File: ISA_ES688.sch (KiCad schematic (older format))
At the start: 90 parts, among them J1 LINE IN, J11 ISA BUS, J2 LINE OUT, J3 Joystick/MIDI, J7 SPKR OUT, J8 MIC, U1 L78L05, U2 74LS14, U7 LM1877, Y1 14.318Mhz

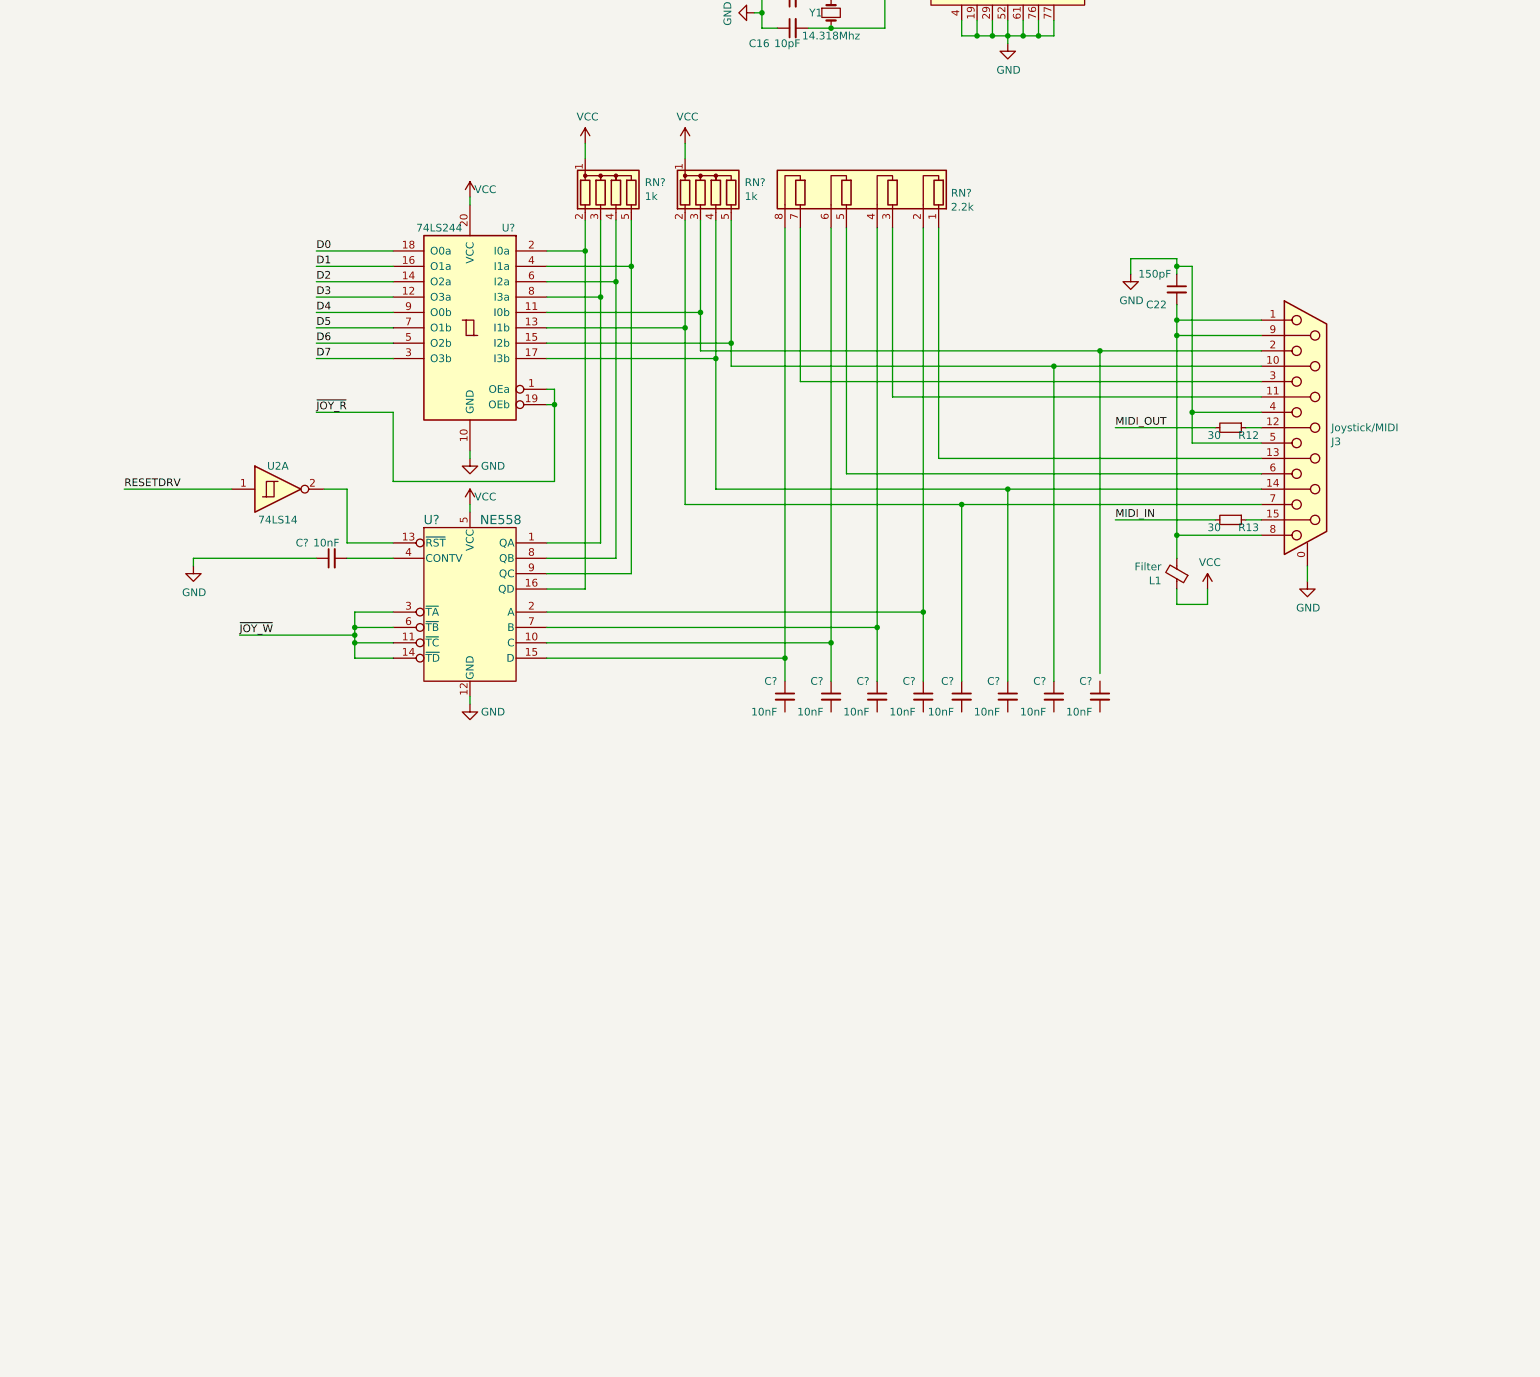
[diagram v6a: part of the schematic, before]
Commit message: Add gnd connection to caps for joystick
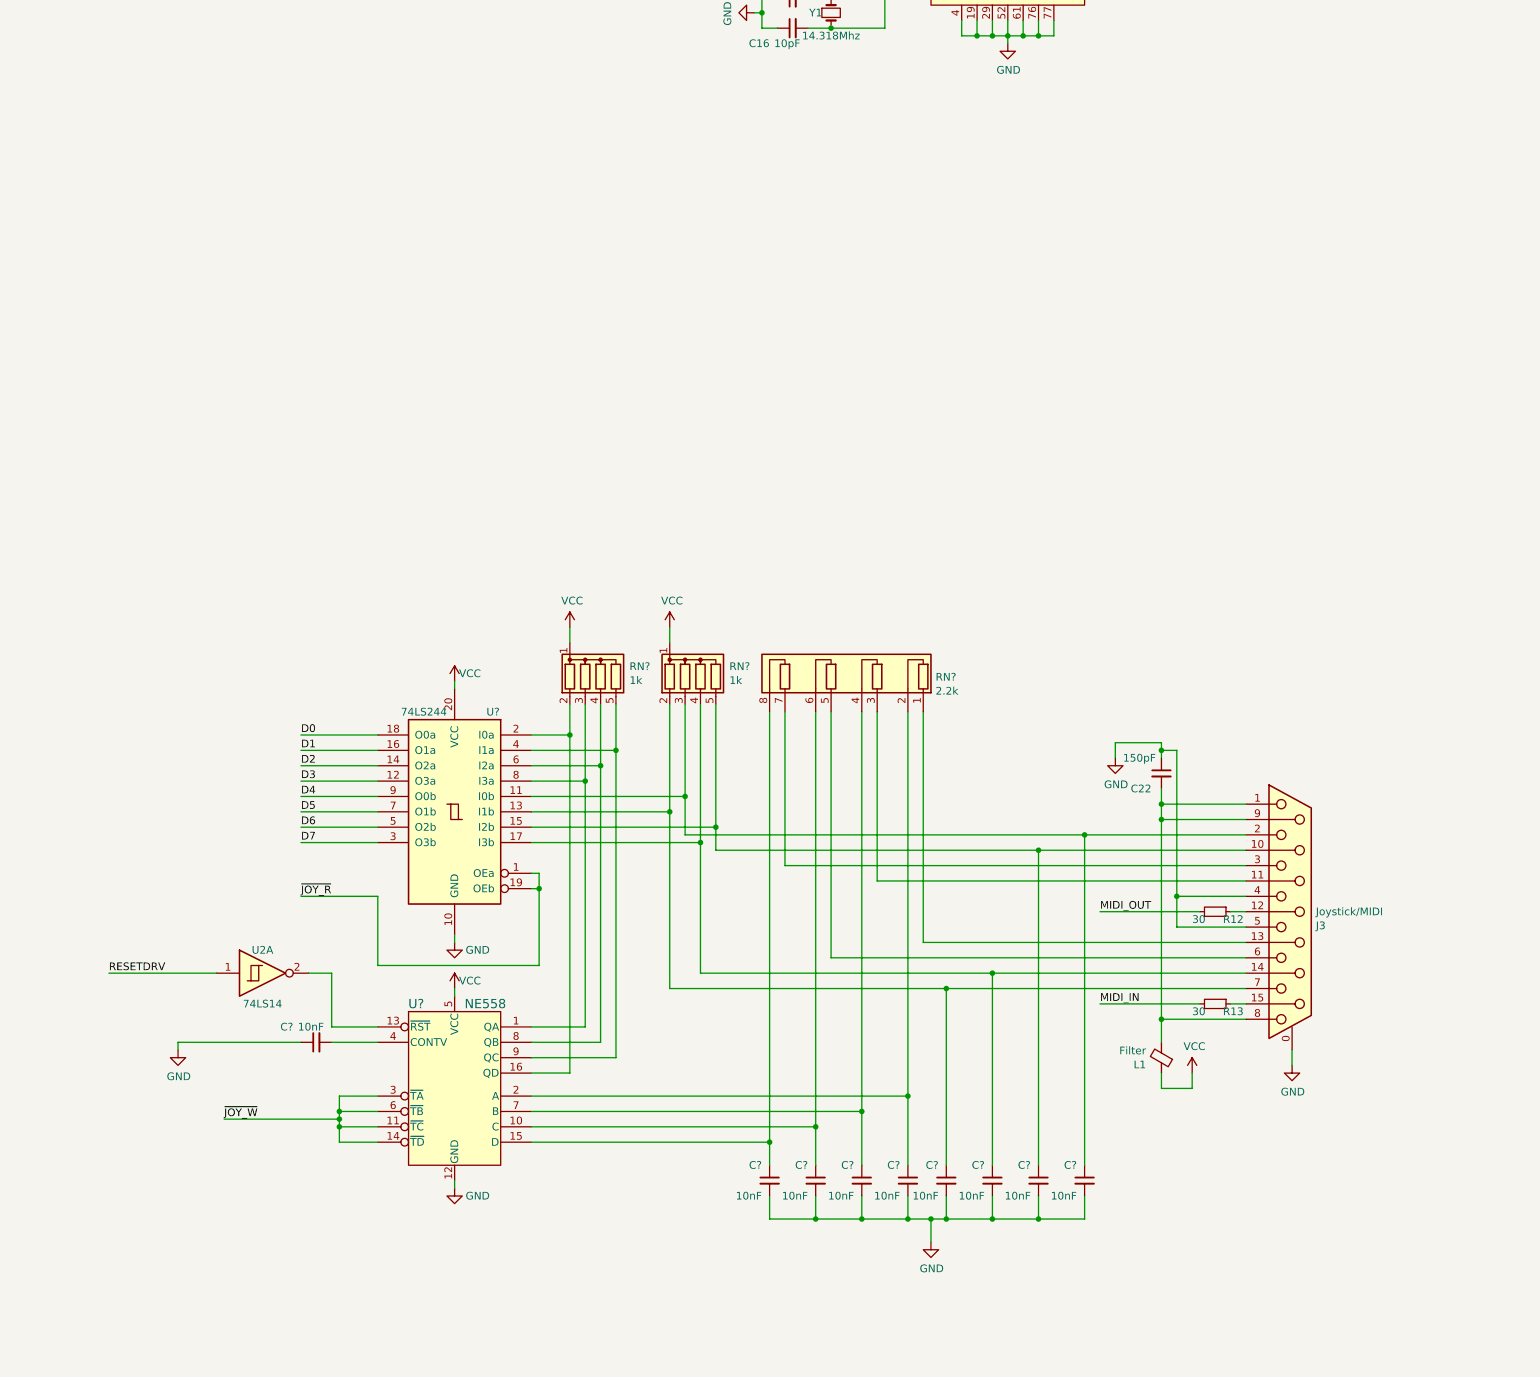
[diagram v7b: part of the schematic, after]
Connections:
- net GND: now also C?.2, C?.2, C?.2, C?.2, C?.2, C?.2, C?.2, C?.2
- net at J3.2, RN?.3 (R2), U?.11 (I0b): now also C?.1
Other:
- moved on the sheet: C22, C?, J3, L1, R12, R13, RN?, U2A, U?

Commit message: Add VDDA symbol
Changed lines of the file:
@@
 Wire Wire Line
 	15350 3200 15450 3200
-Text Label 13300 1850 0    50   ~ 0
-VDDA
 Wire Wire Line
 	14600 5650 15150 5650
@@
 Wire Wire Line
 	11500 14950 11600 14950
+$Comp
+L power:VDDA #PWR?
+U 1 1 674869CE
+P 13850 850
+F 0 "#PWR?" H 13850 700 50  0001 C CNN
+F 1 "VDDA" H 13865 1023 50  0000 C CNN
+F 2 "" H 13850 850 50  0001 C CNN
+F 3 "" H 13850 850 50  0001 C CNN
+	1    13850 850
+	1    0    0    -1
+$EndComp
+Wire Wire Line
+	13850 850  13850 1000
+Connection ~ 13850 1000
 $EndSCHEMATC
